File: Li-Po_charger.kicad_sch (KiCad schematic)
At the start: 36 parts, among them J1 Connector_USB_C, J2 BAT_18650_POS, J3 Output, J4 EXT BAT, J5 BAT_18650_NEG, Q1 FDN340P, SW1 PWR, SW2 BAT_SEL, SW3 VOUT_SEL, U1 TP4056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

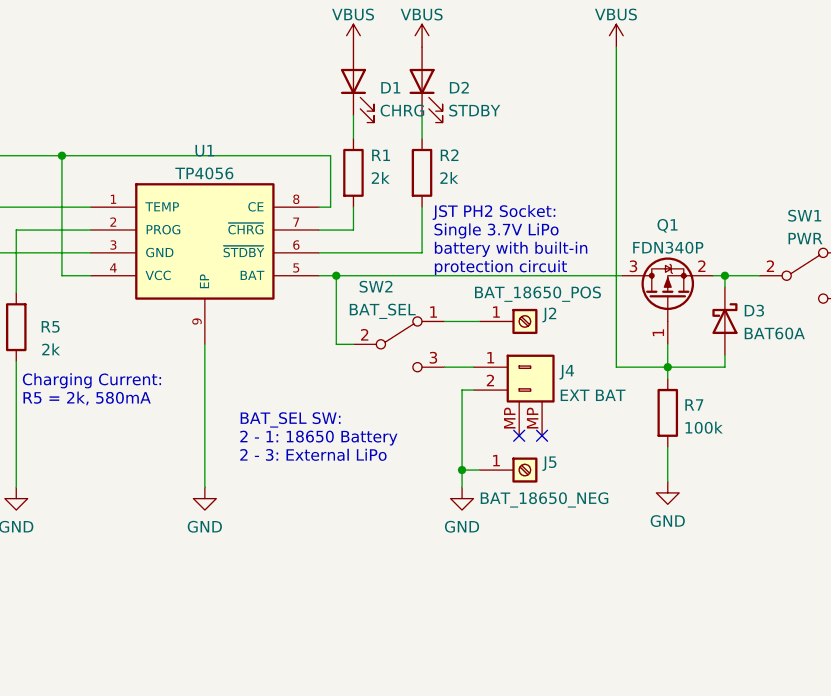
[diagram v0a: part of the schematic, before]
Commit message: Redesign for 18650-only: add P-MOSFET reverse-polarity protection (Q2), remove Li-Po/JST option (SW2, J4), replace TP4056 with LN4056H, update README
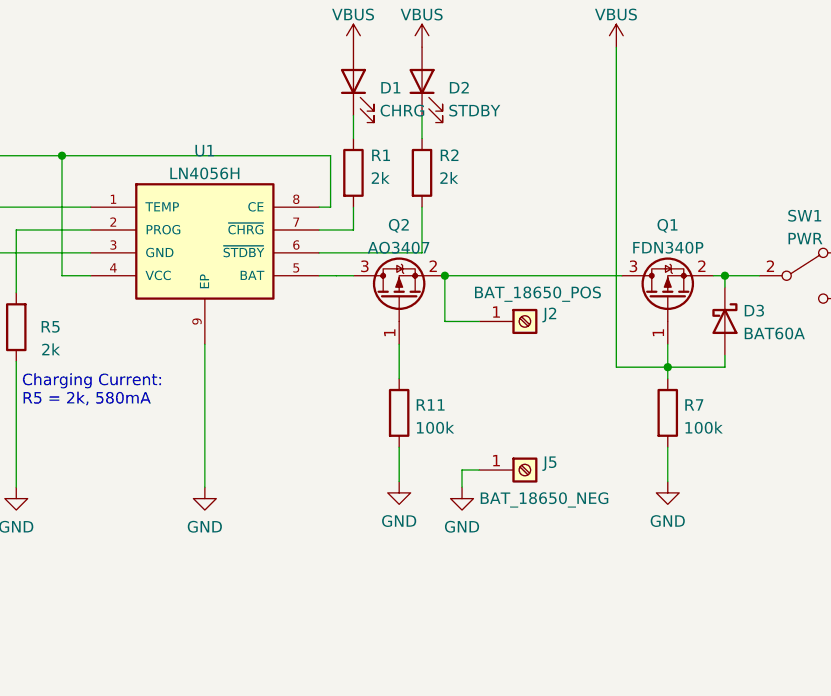
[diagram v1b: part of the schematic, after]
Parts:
- removed J4: EXT BAT, my_library:JST_PH_S2B-PH-SM4-TB_1x02-1MP_P2.00mm_Horizontal, symbol my_library:S2B-PH-SM4-TB
- removed SW2: BAT_SEL, easyeda2kicad:SW_SPDT_MK-12C02-C963206, symbol Switch:SW_SPDT
- added Q2: AO3407, Package_TO_SOT_SMD:SOT-23_Handsoldering, symbol Device:Q_PMOS_GSD
- added R11: 100k, Resistor_SMD:R_0603_1608Metric, symbol Device:R
- U1: value TP4056 -> LN4056H
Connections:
- net GND: now also R11.2
- net at J2.1 (Pin_1): now also Q1.3 (D), Q2.2 (S)
- net at U1.5 (BAT): now also Q2.3 (D); no longer Q1.3 (D)
- new net: Q2.1 (G), R11.1
- no-connect marks 10 -> 8
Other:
- note removed: "BAT_SEL SW: 2 - 1: 18650 Battery 2 - 3: External LiPo"
- note removed: "JST PH2 Socket: Single 3.7V LiPo battery with built-in protection circuit"
- title: LiPo + 18650 Charger with Load Sharing -> 18650 Charger with Load Sharing and Reverse Polarity Protection
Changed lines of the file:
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@@
   (paper "A4")
   (title_block
-    (title "LiPo + 18650 Charger with Load Sharing")
+    (title "18650 Charger with Load Sharing and Reverse Polarity Protection")
     (date "2024-11-12")
     (rev "V1.0")
@@
   (junction (at 205.74 104.775) (diameter 0) (color 0 0 0 0)
   )
-  (junction (at 124.46 118.745) (diameter 0) (color 0 0 0 0)
-  )
   (junction (at 177.8 117.475) (diameter 0) (color 0 0 0 0)
   )
   (junction (at 252.095 94.615) (diameter 0) (color 0 0 0 0)
   )
-  (junction (at 110.49 97.155) (diameter 0) (color 0 0 0 0)
-  )
   (junction (at 80.01 83.82) (diameter 0) (color 0 0 0 0)
   )
@@
   )
   (no_connect (at 167.64 99.695))
-  (no_connect (at 133.35 114.935))
   (no_connect (at 38.1 86.36))
   (no_connect (at 38.1 88.9))
@@
   (no_connect (at 38.1 99.06))
   (no_connect (at 38.1 101.6))
-  (no_connect (at 130.81 114.935))
   (no_connect (at 201.93 99.695))
   (wire (pts (xy 172.72 93.345) (xy 172.72 94.615))
@@
     (stroke (width 0) (type default) (color 0 0 0 0))
   )
-  (wire (pts (xy 112.395 104.775) (xy 110.49 104.775))
-    (stroke (width 0) (type default) (color 0 0 0 0))
-  )
   (wire (pts (xy 172.72 94.615) (xy 172.72 106.045))
     (stroke (width 0) (type default) (color 0 0 0 0))
@@
     (stroke (width 0) (type default) (color 0 0 0 0))
   )
-  (wire (pts (xy 122.555 107.315) (xy 125.73 107.315))
-    (stroke (width 0) (type default) (color 0 0 0 0))
-  )
   (wire (pts (xy 147.32 107.315) (xy 147.32 108.585))
     (stroke (width 0) (type default) (color 0 0 0 0))
@@
     (stroke (width 0) (type default) (color 0 0 0 0))
   )
-  (wire (pts (xy 110.49 104.775) (xy 110.49 97.155))
-    (stroke (width 0) (type default) (color 0 0 0 0))
-  )
   (wire (pts (xy 259.715 102.235) (xy 259.715 103.505))
     (stroke (width 0) (type default) (color 0 0 0 0))
@@
     (stroke (width 0) (type default) (color 0 0 0 0))
   )
-  (wire (pts (xy 124.46 109.855) (xy 124.46 118.745))
-    (stroke (width 0) (type default) (color 0 0 0 0))
-  )
   (wire (pts (xy 153.67 97.155) (xy 157.48 97.155))
     (stroke (width 0) (type default) (color 0 0 0 0))
@@
     (stroke (width 0) (type default) (color 0 0 0 0))
   )
-  (wire (pts (xy 110.49 97.155) (xy 142.24 97.155))
-    (stroke (width 0) (type default) (color 0 0 0 0))
+  (wire (pts (xy 110.49 97.155) (xy 112.395 97.155))
+    (stroke (width 0) (type default) (color 0 0 0 0))
+  )
+  (wire (pts (xy 122.555 97.155) (xy 142.24 97.155))
+    (stroke (width 0) (type default) (color 0 0 0 0))
+  )
+  (wire (pts (xy 122.555 97.155) (xy 122.555 102.235))
+    (stroke (width 0) (type default) (color 0 0 0 0))
+  )
+  (wire (pts (xy 117.475 104.775) (xy 117.475 108.585))
+    (stroke (width 0) (type default) (color 0 0 0 0))
+  )
+  (wire (pts (xy 117.475 116.205) (xy 117.475 120.015))
+    (stroke (width 0) (type default) (color 0 0 0 0))
+  )
+  (junction (at 122.555 97.155) (diameter 0) (color 0 0 0 0)
   )
   (wire (pts (xy 38.1 111.76) (xy 41.91 111.76))
@@
   )
   (wire (pts (xy 234.95 111.125) (xy 234.95 121.285))
-    (stroke (width 0) (type default) (color 0 0 0 0))
-  )
-  (wire (pts (xy 125.73 109.855) (xy 124.46 109.855))
     (stroke (width 0) (type default) (color 0 0 0 0))
   )
@@
     (effects (font (size 1.27 1.27)) (justify left bottom))
   )
-  (text "BAT_SEL SW:\n2 - 1: 18650 Battery\n2 - 3: External LiPo"
-    (at 99.695 118.11 0)
-    (effects (font (size 1.27 1.27)) (justify left bottom))
-  )
   (text "Buck/Boost Converter" (at 198.12 62.23 0)
     (effects (font (size 2.54 2.54)) (justify left bottom))
@@
   (text "Load Sharing" (at 143.51 62.23 0)
     (effects (font (size 2.54 2.54)) (justify left bottom))
-  )
-  (text "JST PH2 Socket:\nSingle 3.7V LiPo\nbattery with built-in\nprotection circuit"
-    (at 121.285 97.155 0)
-    (effects (font (size 1.27 1.27)) (justify left bottom))
   )
   (symbol (lib_id "power:GND") (at 243.205 121.285 0) (unit 1)
@@
     (pin "2")
   )
-  (symbol (lib_id "Switch:SW_SPDT") (at 117.475 104.775 0) (unit 1)
-    (in_bom yes) (on_board yes)
-    (property "Reference" "SW2" (id 0) (at 114.935 98.425 0))
-    (property "Value" "BAT_SEL" (id 1) (at 115.57 100.965 0))
-    (property "Footprint" "easyeda2kicad:SW_SPDT_MK-12C02-C963206" (id 2) (at 117.475 104.775 0)
-      (effects (font (size 1.27 1.27)) hide)
-    )
-    (property "Datasheet" "~" (id 3) (at 117.475 104.775 0)
+  (symbol (lib_id "Device:Q_PMOS_GSD") (at 117.475 99.695 90) (unit 1)
+    (in_bom yes) (on_board yes) (fields_autoplaced)
+    (property "Reference" "Q2" (id 0) (at 117.475 91.5502 90))
+    (property "Value" "AO3407" (id 1) (at 117.475 94.0871 90))
+    (property "Footprint" "Package_TO_SOT_SMD:SOT-23_Handsoldering" (id 2) (at 114.935 94.615 0)
+      (effects (font (size 1.27 1.27)) hide)
+    )
+    (property "Datasheet" "~" (id 3) (at 117.475 99.695 0)
       (effects (font (size 1.27 1.27)) hide)
     )
@@
     (pin "2")
     (pin "3")
+  )
+  (symbol (lib_id "Device:R") (at 117.475 112.395 0) (unit 1)
+    (in_bom yes) (on_board yes) (fields_autoplaced)
+    (property "Reference" "R11" (id 0) (at 119.253 111.5603 0)
+      (effects (font (size 1.27 1.27)) (justify left))
+    )
+    (property "Value" "100k" (id 1) (at 119.253 114.0972 0)
+      (effects (font (size 1.27 1.27)) (justify left))
+    )
+    (property "Footprint" "Resistor_SMD:R_0603_1608Metric" (id 2) (at 115.697 112.395 90)
+      (effects (font (size 1.27 1.27)) hide)
+    )
+    (property "Datasheet" "~" (id 3) (at 117.475 112.395 0)
+      (effects (font (size 1.27 1.27)) hide)
+    )
+    (pin "1")
+    (pin "2")
+  )
+  (symbol (lib_id "power:GND") (at 117.475 120.015 0) (unit 1)
+    (in_bom yes) (on_board yes) (fields_autoplaced)
+    (property "Reference" "#PWR022" (id 0) (at 117.475 126.365 0)
+      (effects (font (size 1.27 1.27)) hide)
+    )
+    (property "Value" "GND" (id 1) (at 117.475 124.4584 0))
+    (property "Footprint" "" (id 2) (at 117.475 120.015 0)
+      (effects (font (size 1.27 1.27)) hide)
+    )
+    (property "Datasheet" "" (id 3) (at 117.475 120.015 0)
+      (effects (font (size 1.27 1.27)) hide)
+    )
+    (pin "1")
   )
   (symbol (lib_id "Device:Q_PMOS_GSD") (at 147.32 99.695 90) (unit 1)
@@
     (pin "2")
   )
-  (symbol (lib_id "my_library:S2B-PH-SM4-TB") (at 132.08 107.315 0) (unit 1)
-    (in_bom yes) (on_board yes)
-    (property "Reference" "J4" (id 0) (at 135.382 107.7503 0)
-      (effects (font (size 1.27 1.27)) (justify left))
-    )
-    (property "Value" "EXT BAT" (id 1) (at 135.255 110.49 0)
-      (effects (font (size 1.27 1.27)) (justify left))
-    )
-    (property "Footprint" "my_library:JST_PH_S2B-PH-SM4-TB_1x02-1MP_P2.00mm_Horizontal" (id 2) (at 132.08 107.315 0)
-      (effects (font (size 1.27 1.27)) hide)
-    )
-    (property "Datasheet" "~" (id 3) (at 130.81 107.315 0)
-      (effects (font (size 1.27 1.27)) hide)
-    )
-    (pin "1")
-    (pin "2")
-    (pin "MP")
-    (pin "MP")
-  )
   (symbol (lib_id "Device:C") (at 243.205 107.315 0) (unit 1)
     (in_bom yes) (on_board yes)
@@
     (in_bom yes) (on_board yes) (fields_autoplaced)
     (property "Reference" "U1" (id 0) (at 95.885 83.2952 0))
-    (property "Value" "TP4056" (id 1) (at 95.885 85.8321 0))
+    (property "Value" "LN4056H" (id 1) (at 95.885 85.8321 0))
     (property "Footprint" "my_library:SOP127P600X175-9N" (id 2) (at 98.425 93.345 0)
       (effects (font (size 1.27 1.27)) (justify bottom) hide)
@@
       (reference "#PWR021") (unit 1) (value "GND") (footprint "")
     )
+    (path "/ac2a4a36-ae0a-4331-979c-36c9331f19c6"
+      (reference "#PWR022") (unit 1) (value "GND") (footprint "")
+    )
     (path "/0a5ee5f2-10e4-4ac7-9d1e-e54116e725ce"
       (reference "C1") (unit 1) (value "0.1uF") (footprint "Capacitor_SMD:C_0603_1608Metric")
@@
       (reference "J3") (unit 1) (value "Output") (footprint "Connector_PinSocket_2.54mm:PinSocket_1x02_P2.54mm_Vertical")
     )
-    (path "/82dbc478-9224-4ae1-b4d1-bb10bc1d855f"
-      (reference "J4") (unit 1) (value "EXT BAT") (footprint "my_library:JST_PH_S2B-PH-SM4-TB_1x02-1MP_P2.00mm_Horizontal")
-    )
     (path "/8cb699f2-58f7-408d-884d-90c8c647c062"
       (reference "J5") (unit 1) (value "BAT_18650_NEG") (footprint "easyeda2kicad:BAT-SMD_MY-18650-02")
@@
       (reference "L1") (unit 1) (value "0.47uH") (footprint "Inductor_SMD:L_Taiyo-Yuden_NR-50xx_HandSoldering")
     )
+    (path "/178ee2b2-f60e-4713-9ed7-122e3fdd6eb7"
+      (reference "Q2") (unit 1) (value "AO3407") (footprint "Package_TO_SOT_SMD:SOT-23_Handsoldering")
+    )
     (path "/2865b647-bf37-4783-b377-d83bd0f28a16"
       (reference "Q1") (unit 1) (value "FDN340P") (footprint "Package_TO_SOT_SMD:SOT-23_Handsoldering")
@@
       (reference "R10") (unit 1) (value "2k") (footprint "Resistor_SMD:R_0603_1608Metric")
     )
+    (path "/0dab7609-a582-45ad-afdc-781c0228ee1d"
+      (reference "R11") (unit 1) (value "100k") (footprint "Resistor_SMD:R_0603_1608Metric")
+    )
     (path "/ae30af75-679f-4e71-b6a7-b2647223580b"
       (reference "SW1") (unit 1) (value "PWR") (footprint "easyeda2kicad:SW_SPDT_MK-12C02-C963206")
     )
-    (path "/276b22bd-eb80-434f-9352-958c106ab342"
-      (reference "SW2") (unit 1) (value "BAT_SEL") (footprint "easyeda2kicad:SW_SPDT_MK-12C02-C963206")
-    )
     (path "/64859ad6-41fa-446a-8dde-33ac71015174"
       (reference "SW3") (unit 1) (value "VOUT_SEL") (footprint "Button_Switch_SMD:SW_DIP_SPSTx01_Slide_Copal_CHS-01A_W5.08mm_P1.27mm_JPin")
     )
     (path "/c8050d36-479e-4efc-a2b8-ea2887cd39a3"
-      (reference "U1") (unit 1) (value "TP4056") (footprint "my_library:SOP127P600X175-9N")
+      (reference "U1") (unit 1) (value "LN4056H") (footprint "my_library:SOP127P600X175-9N")
     )
     (path "/8858d596-b1d3-4897-8279-3e1676236e06"
